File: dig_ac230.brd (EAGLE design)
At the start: 100 x 85 mm, 142 parts, among them IC201 ATMEGA32A-AU, IC202 DS1337S, IC203 MAX487CSA, IC204 74HC166D, IC301 LTV-356T, IC302 LTV-356T, IC303 LTV-356T, IC304 LTV-356T, IC305 LTV-356T, IC306 LTV-356T, IC307 LTV-356T, IC308 LTV-356T, IC401 74HC595D, K401 S202S02, K402 S202S02, K403 S202S02, K404 S202S02, K405 S202S02, K406 S202S02, K407 S202S02, K408 S202S02, Q201 32,768kHz, Q301 BCR191, Q302 BCR191, Q303 BCR191, Q304 BCR191, Q305 BCR191, Q306 BCR191, Q307 BCR191, Q308 BCR191, X101 RIA-73-02, X201 ISP, X202 RIA-73-02, X301 RIA-73-02, X302 RIA-73-02, X303 RIA-73-02, X304 RIA-73-02, X305 RIA-73-02, X401 RIA-73-02, X402 RIA-73-02, X403 RIA-73-02, X404 RIA-73-02, X405 RIA-73-02

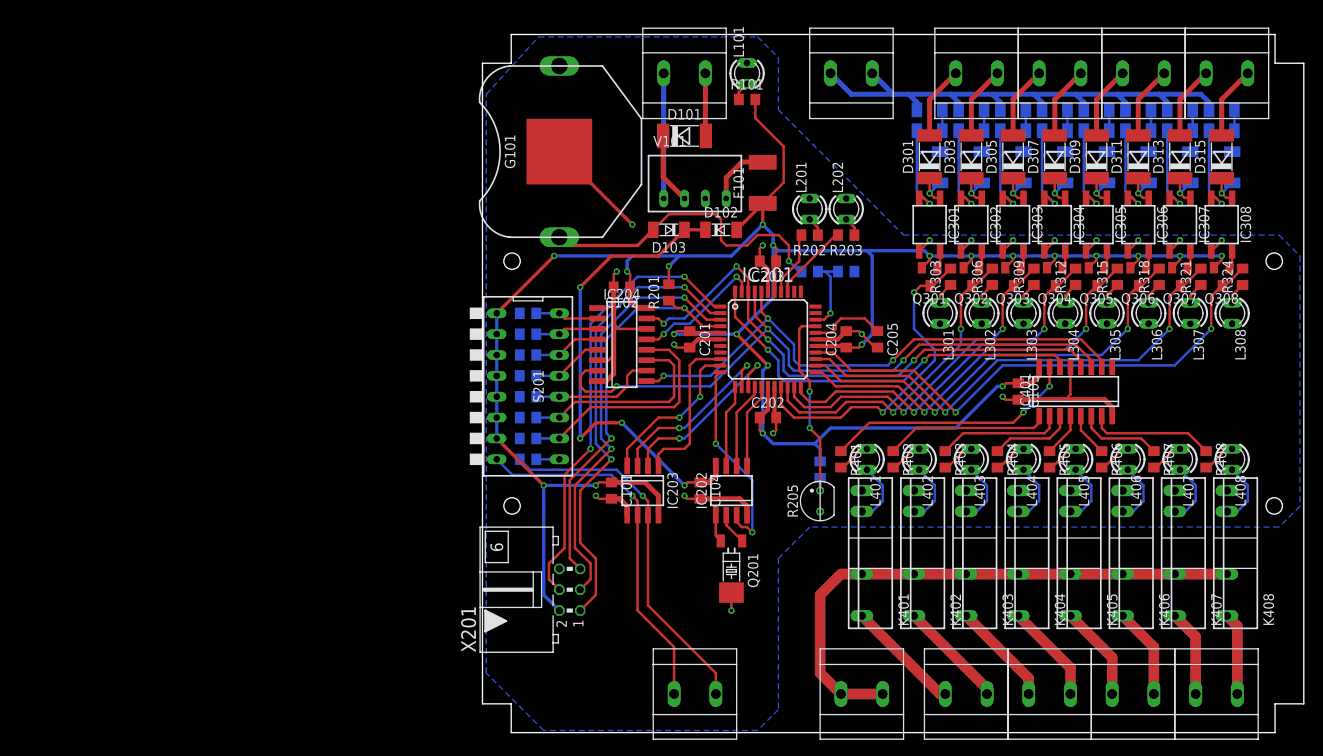
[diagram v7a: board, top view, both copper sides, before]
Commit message: Bauteile wegen Beschriftung ausgetauscht
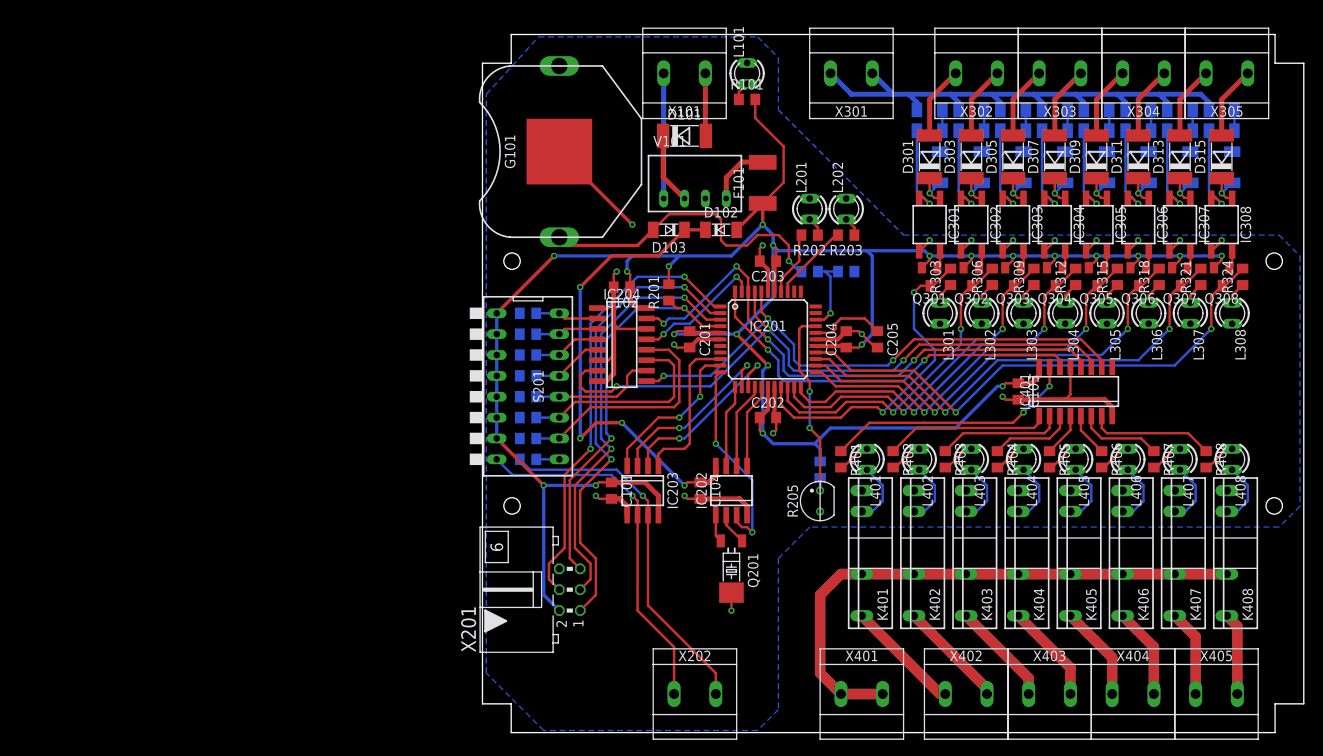
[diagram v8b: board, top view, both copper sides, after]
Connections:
- net N renamed GNDIO
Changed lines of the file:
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@@
 <wire x1="22.225" y1="34.925" x2="22.225" y2="32.845" width="0.3048" layer="1"/>
 </signal>
-<signal name="N">
+<signal name="GNDIO">
 <contactref element="R308" pad="1"/>
 <contactref element="R302" pad="1"/>
